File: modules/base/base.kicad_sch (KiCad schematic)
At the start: 83 parts, among them J1 LineOut, J2 Ground, J23 PZ200-1-02-Z, J4 Ground, J5 USB_C_Receptacle_PowerOnly_6P, J6 HeadphoneOut, SW1 K2-1808SN-A4SW-01, U18 TS5A23157DGS, U2 MCP6002-xSN, U3 TS922IDT, U4 MCP6002-xSN, U5 AP2112K-3.3

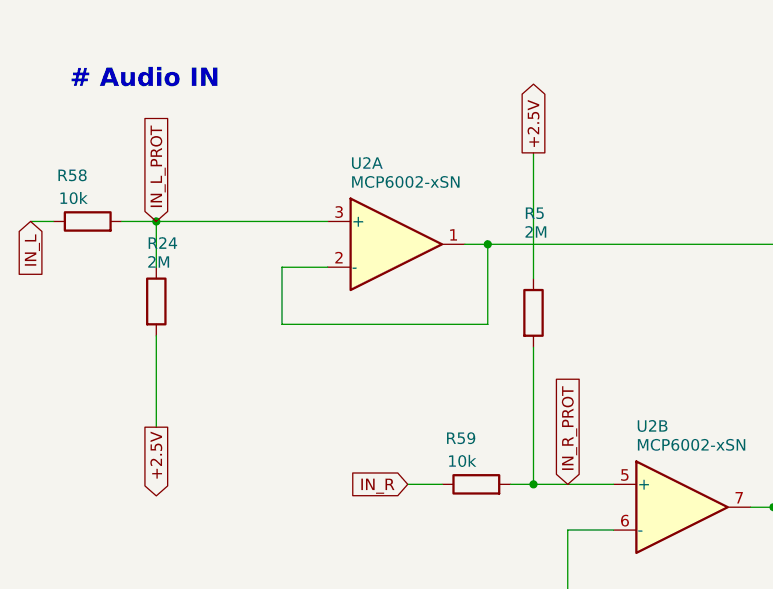
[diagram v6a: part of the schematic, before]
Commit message: Checkpoint verified base input routing and production mirrors
Preserve the completed main-checkout R5/R60 and R24/R61 1M series input routing, C46 100uF 1206 C15008, synchronized supplier metadata and exact production mirrors.

Private exact-source verification: 0 DRC errors/unconnected/parity; 73 library-copy warnings retained. ERC baseline unchanged: 7 errors and 4 symbol-library warnings. 33 BOM rows / 117 refs; source and mirrored payload hashes verified.

52 exporter/wrapper tests and 6 datum tests pass on real fixtures. Only obsolete base test totals changed (115/35 to 117/33). Preserve wrapper/README/tests and record scoped verification without changing circuit geometry, project rules or waivers.

R18/R19 680k remain Preferred Extended, not Basic; no Economy/order approval claim. Exclude unrelated nested history repositories and isolated sourcing-worker work.
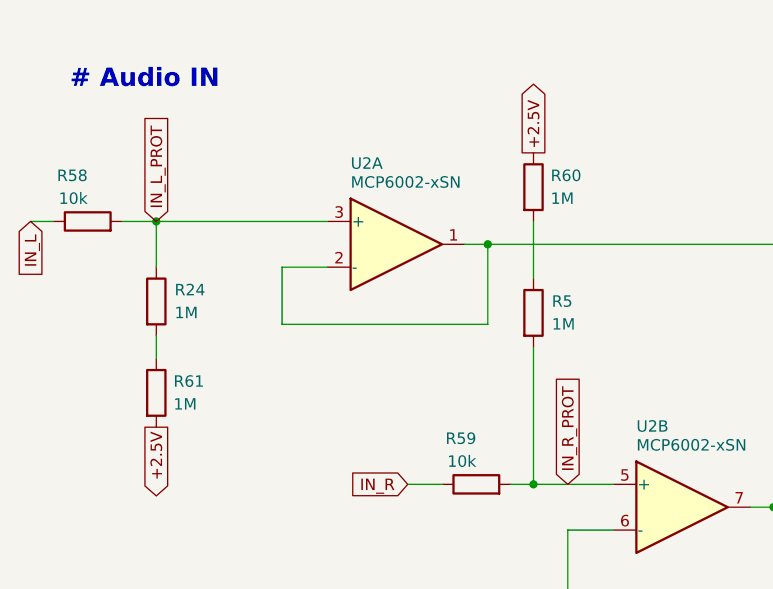
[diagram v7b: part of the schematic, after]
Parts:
- added R60, R61: 1M, Resistor_SMD:R_0402_1005Metric, symbol Device:R
- C1, C10, C11, C12, C13, C14, C15, C16, C2, C20, C21, C3, C4, C50, C51, C52, C7, C8, C9: Manufacturer Samsung -> Samsung Electro-Mechanics
- C17, C6: LCSC C90146 -> C12891; MPN CL31A226KOHNNNE -> CL31A226KAHNNNE; Manufacturer Samsung -> Samsung Electro-Mechanics
- C18, C19: LCSC C1705 -> C19666; MPN CL10A475KP8NNNC -> CL10A475KO8NNNC; Manufacturer Samsung -> Samsung Electro-Mechanics
- C46: footprint Capacitor_SMD:C_1210_3225Metric -> Capacitor_SMD:C_1206_3216Metric; LCSC C394395 -> C15008; MPN EMK325ABJ107MM-T -> CL31A107MQHNNNE; Manufacturer (none) -> Samsung Electro-Mechanics
- C5: LCSC C472806 -> C1710; MPN CL21B103KB6WPNC -> CL21B103KBANNNC; Manufacturer Samsung -> Samsung Electro-Mechanics
- R1, R10, R12, R14, R15, R16, R17, R18, R19, R2, R20, R21, R26, R27, R3, R4, R55, R57, R58, R59, R6, R7, R8, R9: Manufacturer UNI-ROYAL -> UNI-ROYAL(Uniroyal Elec)
- R24, R5: value 2M -> 1M; LCSC C11512 -> C26083; MPN 0402WGF2004TCE -> 0402WGF1004TCE; Manufacturer UNI-ROYAL -> UNI-ROYAL(Uniroyal Elec)
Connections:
- net +2.5V: now also R60.1, R61.2; no longer R24.2, R5.1
- new net: R24.2, R61.1
- new net: R5.1, R60.2

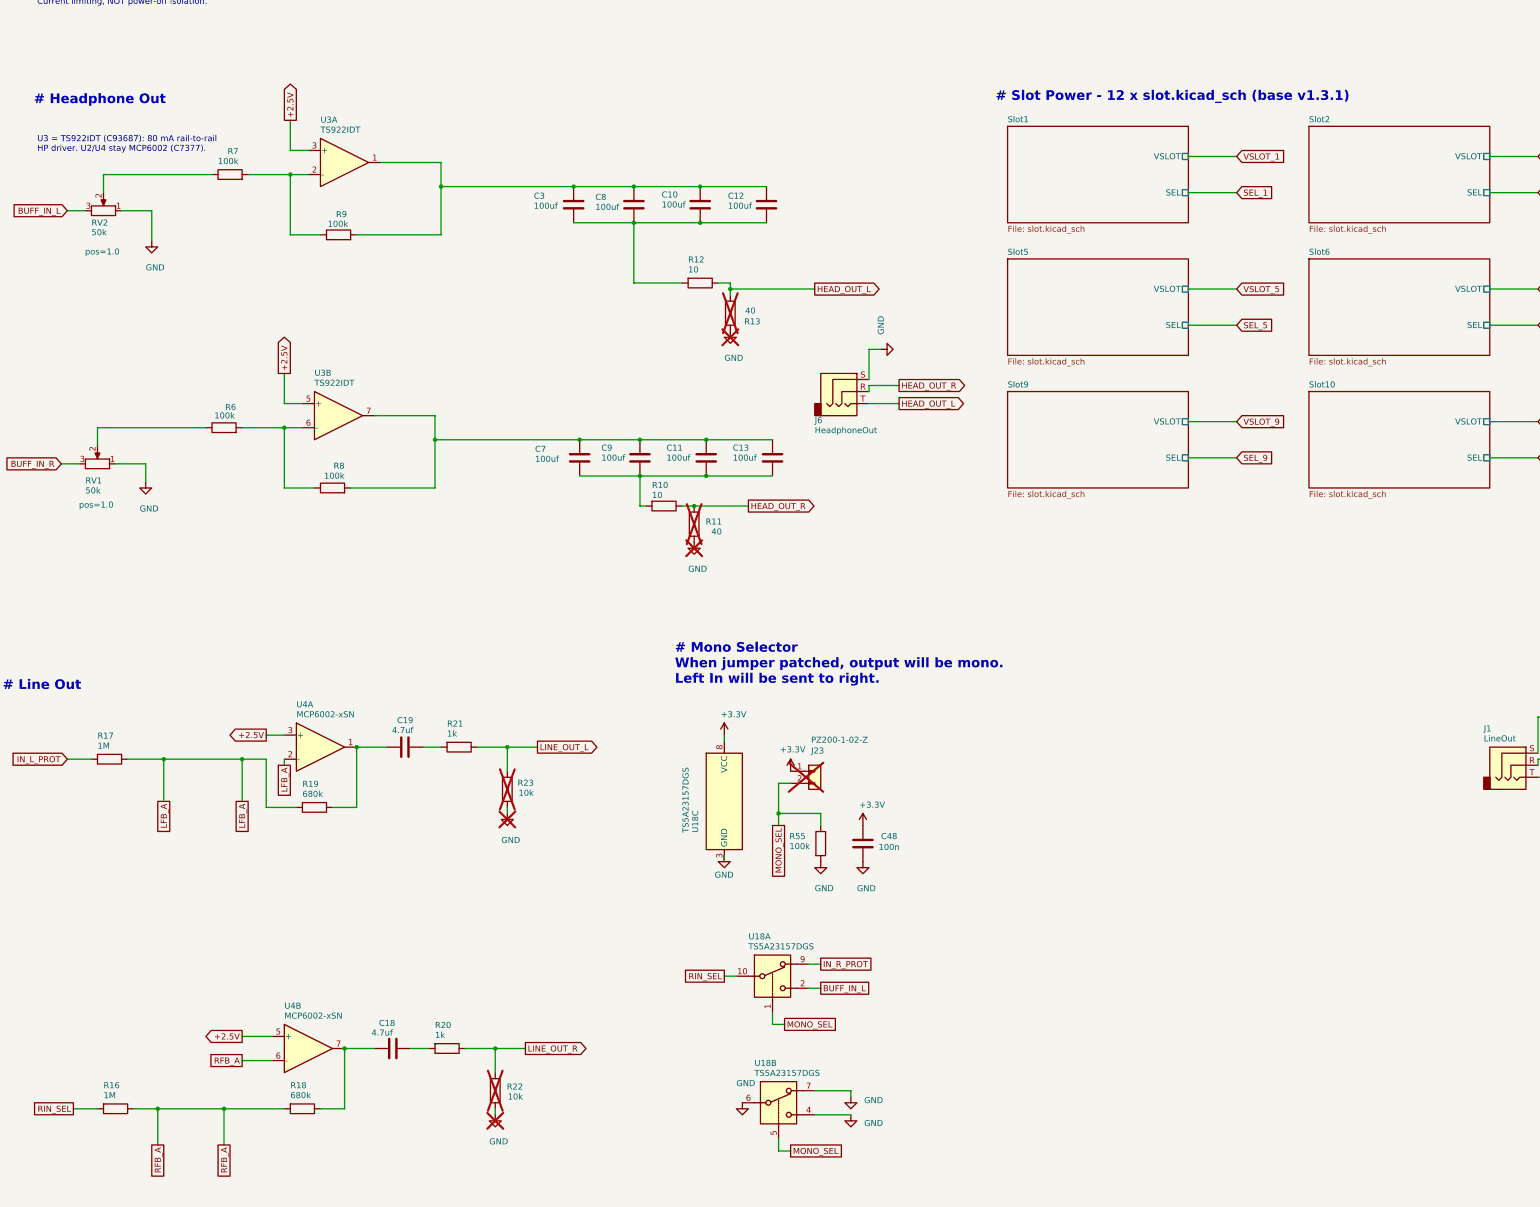
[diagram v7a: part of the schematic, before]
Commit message: Add a switch for 5V and MONO selector.
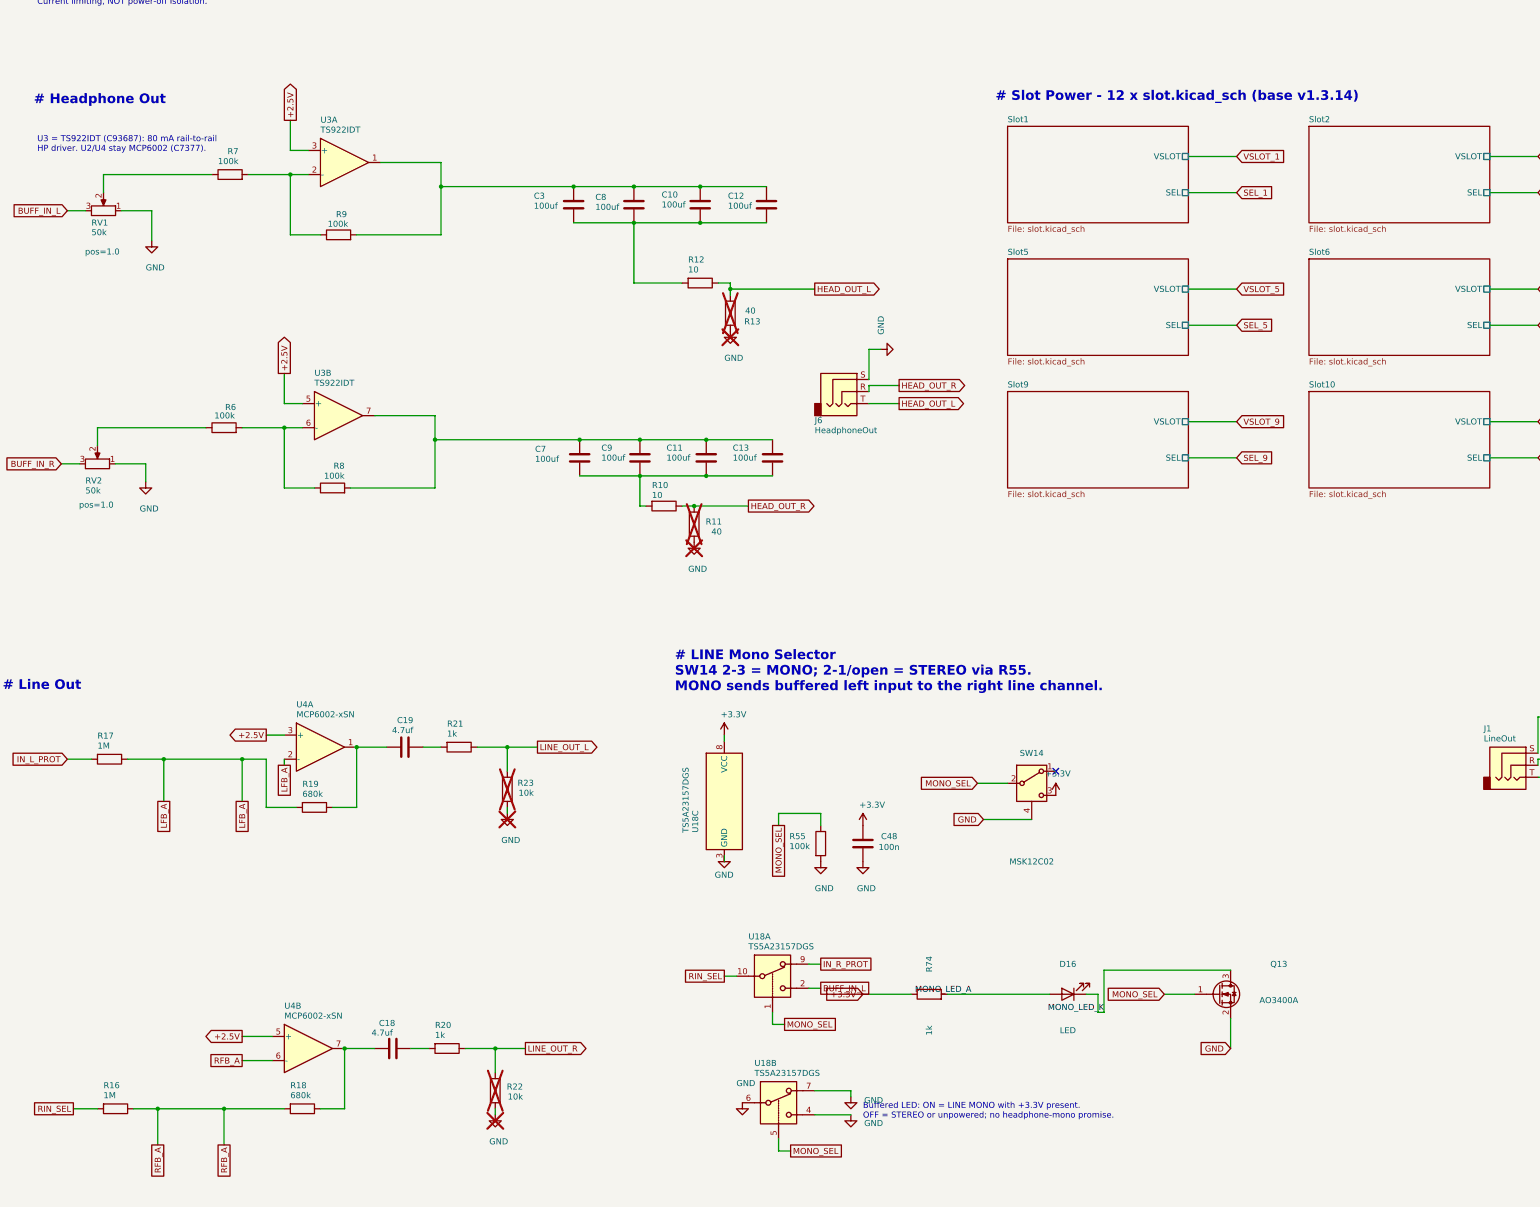
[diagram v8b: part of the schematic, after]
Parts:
- removed J23: PZ200-1-02-Z, Connector_PinHeader_2.00mm:PinHeader_1x02_P2.00mm_Vertical, symbol Connector_Generic:Conn_01x02
- added D16: LED, LED_SMD:LED_0603_1608Metric, symbol BreadModular_Selectors:Indicator_LED
- added Q13: AO3400A, Package_TO_SOT_SMD:SOT-23, symbol Transistor_FET:Q_NMOS_GSD
- added R74: 1k, Resistor_SMD:R_0402_1005Metric, symbol Device:R
- added SW14: MSK12C02, BreadModular_Selectors:SW_SPDT_Shouhan_MSK12C02_C431540, symbol BreadModular_Selectors:MSK12C02
- D1: Manufacturer Harvatek -> Hubei KENTO Elec
- renumbered RV2 to RV1, RV1 to RV2
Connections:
- net +3.3V: now also R74.1, SW14.3 (C)
- net GND: now also Q13.2 (S), SW14.4 (SHIELD)
- net MONO_SEL: now also Q13.1 (G), SW14.2 (B)
- new net MONO_LED_A: D16.2 (A), R74.2
- new net MONO_LED_K: D16.1 (K), Q13.3 (D)
- no-connect marks 0 -> 1
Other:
- note added: "# LINE Mono Selector SW14 2-3 = MONO; 2-1/open = STEREO via R55. MONO sends buffered left input to the right line channel."
- note added: "# Slot Power - 12 x slot.kicad_sch (base v1.3.14)"
- note added: "Buffered LED: ON = LINE MONO with +3.3V present. OFF = STEREO or unpowered; no headphone-mono promise."
- note removed: "# Mono Selector When jumper patched, output will be mono. Left In will be sent to right."
- note removed: "# Slot Power - 12 x slot.kicad_sch (base v1.3.1)"
